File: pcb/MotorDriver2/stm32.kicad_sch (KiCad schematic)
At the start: 21 parts, among them IC1 STM32C092RCT6, SW1 K2-6639SP-C4SC-04, SW2 K2-6639SP-C4SC-04, SW3 K2-6639SP-C4SC-04, Y1 48 MHz, Y2 32.768 kHz

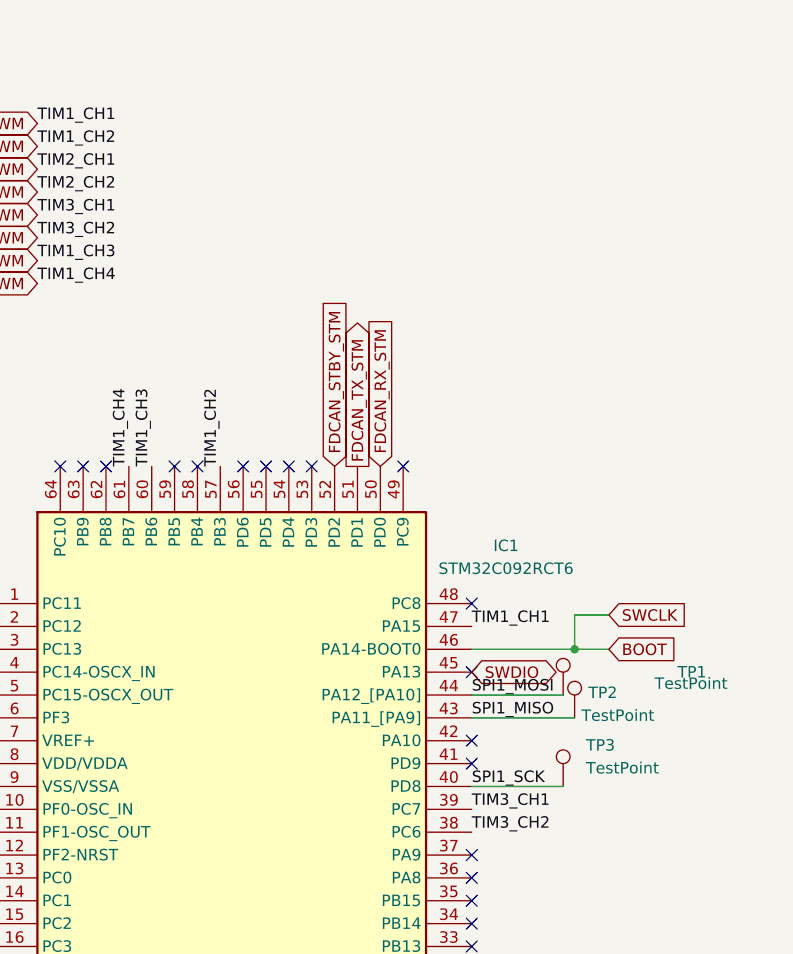
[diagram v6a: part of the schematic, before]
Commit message: Removed can transceivers, replaced with spi
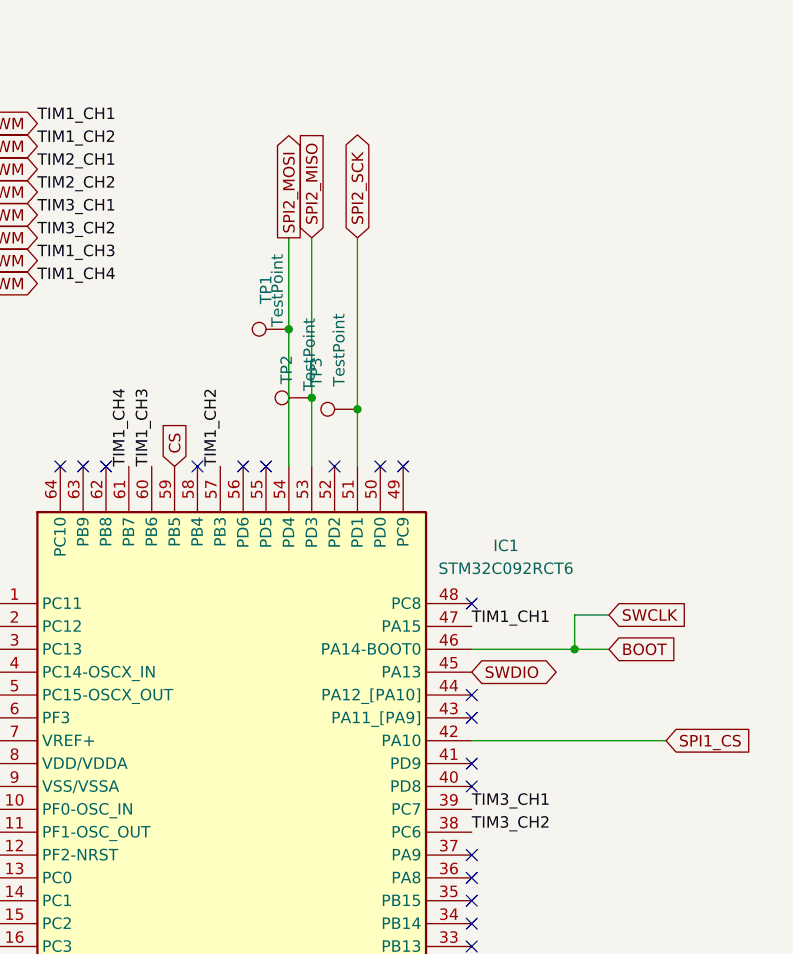
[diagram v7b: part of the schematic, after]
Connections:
- net SPI1_CS: now reaches IC1.42 (PA10)
- net SPI2_MISO: now reaches IC1.53 (PD3)
- net SPI2_MISO: now also TP2.1
- net SPI2_MOSI: now reaches IC1.54 (PD4)
- net SPI2_MOSI: now also TP1.1
- net CS: now reaches IC1.59 (PB5)
- net FDCAN_RX_STM: no longer names the net of IC1.50 (PD0)
- net FDCAN_STBY_STM: no longer names the net of IC1.52 (PD2)
- net FDCAN_TX_STM renamed SPI2_SCK
- net SPI2_SCK: now also TP3.1
- net SPI1_MISO: no longer names the net of IC1.43 (PA11_[PA9])
- net SPI1_MISO: no longer TP2.1
- net SPI1_MOSI: no longer names the net of IC1.44 (PA12_[PA10])
- net SPI1_MOSI: no longer TP1.1
- net SPI1_SCK: no longer names the net of IC1.40 (PD8)
- net SPI1_SCK: no longer TP3.1
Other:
- moved on the sheet: TP1, TP2, TP3
